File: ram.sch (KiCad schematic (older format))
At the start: 16 parts, among them U10 41256, U11 41256, U12 41256, U13 41256, U14 41256, U7 41256, U8 41256, U9 41256

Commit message: Routing in progress
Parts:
- removed C10, C11, C12, C13, C14, C8, C9: 100n, Capacitor_SMD:C_0805_2012Metric_Pad1.18x1.45mm_HandSolder, symbol Device:C
- removed U10, U11, U12, U13, U14, U7, U8, U9: 41256, Package_DIP:DIP-16_W7.62mm_Socket, symbol 41256:41256
- added U6: AS6C4008, Package_DIP:DIP-32_W15.24mm_Socket_LongPads, symbol AS6C4008:AS6C4008
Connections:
- net labels added: a0, a1, a10, a11, a12, a13, a14, a15, a16, a17, a18, a2, a3, a4, a5, a6, a7, a8, a9, a[0..18], ~SRAM_CE, ~sram_ce
- net labels removed: MultiplexedAddressBus, m0, m1, m2, m3, m4, m5, m6, m7, m8, m[0..8], ~CAS_64K, ~RAS
- wire segments 218 -> 40
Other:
- note removed: "WE NEED TO USE 41256 RAM CHIPS AS THEIR INTERNAL MATRIX IS\nORGANIZED IN 256 ROWS BY 1024 COLUMNS AND THUS ONLY NEED\nROWS A0-A7 FOR RAS-ONLY REFRESH (WHICH IS WHAT TED PRODUCES).\n\n44256 ARE GENERALLY ORGANIZED IN 512 ROWS AND WOULD NEED\nA MUCH MORE COMPLEX REFRESH LOGIC, IN ORDER TO REFRESH THE\nPAGES THAT ARE CURRENTLY NOT SELECTED."
- moved on the sheet: C7

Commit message: More routing
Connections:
- net d0: now also U6.15 (D2); no longer U6.13 (D0)
- net d2: now also U6.13 (D0); no longer U6.15 (D2)
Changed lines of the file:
@@
 d[0..7]
 Text Label 7340 4740 0    50   ~ 0
-d0
+d2
 Text Label 7340 4840 0    50   ~ 0
 d1
 Text Label 7340 4940 0    50   ~ 0
-d2
-Text Label 9730 4640 2    50   ~ 0
-d7
-Text Label 9730 4740 2    50   ~ 0
-d6
+d0
 Text Label 9730 4840 2    50   ~ 0
 d5
@@
 Wire Wire Line
 	9380 4540 9775 4540
+Text Label 9730 4040 2    50   ~ 0
+a6
+Text Label 9730 4240 2    50   ~ 0
+a4
 Wire Bus Line
 	7240 4640 7240 5670
@@
 Wire Bus Line
 	7240 2895 7240 4540
-Text Label 9730 4040 2    50   ~ 0
-a6
-Text Label 9730 4240 2    50   ~ 0
-a4
+Text Label 9730 4740 2    50   ~ 0
+d6
+Text Label 9730 4640 2    50   ~ 0
+d7
 $EndSCHEMATC

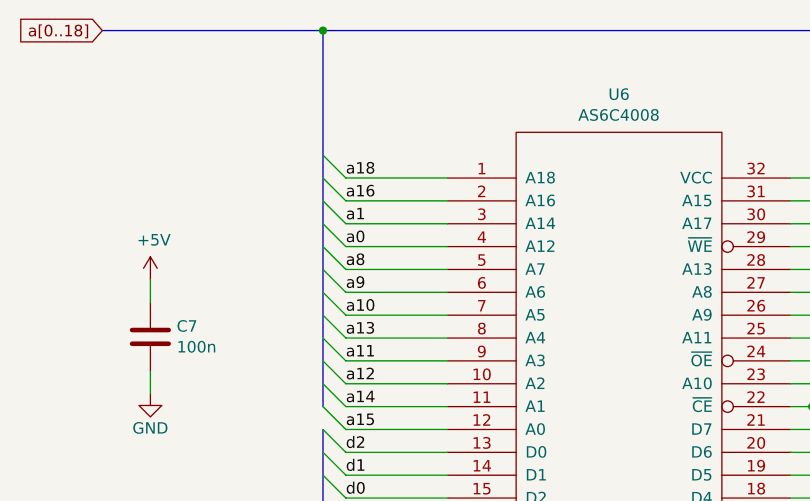
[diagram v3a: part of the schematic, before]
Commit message: Relabel all components
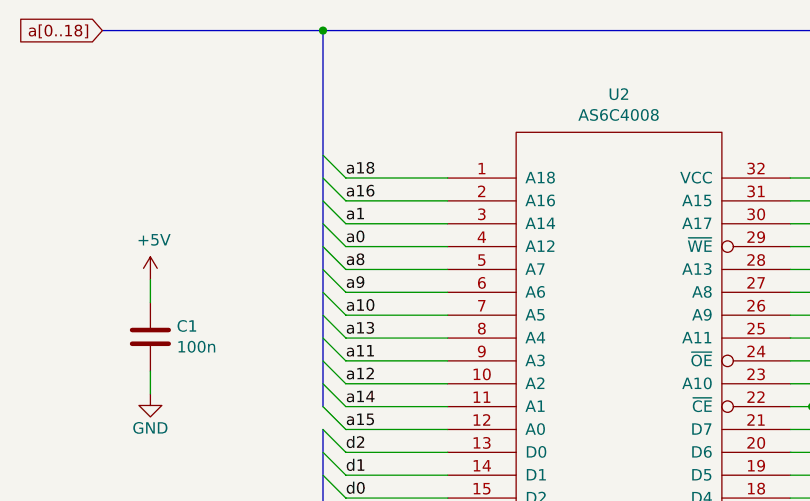
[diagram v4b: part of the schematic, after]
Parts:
- renumbered C7 to C1, U6 to U2
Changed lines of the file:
@@
 P 6485 4235
 AR Path="/63BD05FA" Ref="C?"  Part="1"
-AR Path="/62E48B71/63BD05FA" Ref="C7"  Part="1"
+AR Path="/62E48B71/63BD05FA" Ref="C1"  Part="1"
 AR Path="/63A22C28/63BD05FA" Ref="C?"  Part="1"
-F 0 "C7" H 6600 4281 50  0000 L CNN
+F 0 "C1" H 6600 4281 50  0000 L CNN
 F 1 "100n" H 6600 4190 50  0000 L CNN
 F 2 "Capacitor_SMD:C_0805_2012Metric_Pad1.18x1.45mm_HandSolder" H 6523 4085 50  0001 C CNN
@@
 P 6485 4485
 AR Path="/63BD0600" Ref="#PWR?"  Part="1"
-AR Path="/62E48B71/63BD0600" Ref="#PWR06"  Part="1"
+AR Path="/62E48B71/63BD0600" Ref="#PWR07"  Part="1"
 AR Path="/63A22C28/63BD0600" Ref="#PWR?"  Part="1"
-F 0 "#PWR06" H 6485 4235 50  0001 C CNN
+F 0 "#PWR07" H 6485 4235 50  0001 C CNN
 F 1 "GND" H 6485 4335 50  0000 C CNN
 F 2 "" H 6485 4485 50  0001 C CNN
@@
 P 6485 3985
 AR Path="/63BD0608" Ref="#PWR?"  Part="1"
-AR Path="/62E48B71/63BD0608" Ref="#PWR03"  Part="1"
+AR Path="/62E48B71/63BD0608" Ref="#PWR06"  Part="1"
 AR Path="/63A22C28/63BD0608" Ref="#PWR?"  Part="1"
-F 0 "#PWR03" H 6485 3835 50  0001 C CNN
+F 0 "#PWR06" H 6485 3835 50  0001 C CNN
 F 1 "+5V" H 6500 4158 50  0000 C CNN
 F 2 "" H 6485 3985 50  0001 C CNN
@@
 $EndComp
 $Comp
-L AS6C4008:AS6C4008 U6
+L AS6C4008:AS6C4008 U2
 U 1 1 63F5A21F
 P 8535 4290
-F 0 "U6" H 8535 5405 50  0000 C CNN
+F 0 "U2" H 8535 5405 50  0000 C CNN
 F 1 "AS6C4008" H 8535 5314 50  0000 C CNN
 F 2 "Package_DIP:DIP-32_W15.24mm_Socket_LongPads" H 8535 4290 50  0001 C CNN
@@
 P 7605 5385
 AR Path="/63FAC74C" Ref="#PWR?"  Part="1"
-AR Path="/62E48B71/63FAC74C" Ref="#PWR07"  Part="1"
+AR Path="/62E48B71/63FAC74C" Ref="#PWR08"  Part="1"
 AR Path="/63A22C28/63FAC74C" Ref="#PWR?"  Part="1"
-F 0 "#PWR07" H 7605 5135 50  0001 C CNN
+F 0 "#PWR08" H 7605 5135 50  0001 C CNN
 F 1 "GND" H 7605 5235 50  0000 C CNN
 F 2 "" H 7605 5385 50  0001 C CNN
@@
 P 9465 3195
 AR Path="/6400E4BF" Ref="#PWR?"  Part="1"
-AR Path="/62E48B71/6400E4BF" Ref="#PWR08"  Part="1"
+AR Path="/62E48B71/6400E4BF" Ref="#PWR09"  Part="1"
 AR Path="/63A22C28/6400E4BF" Ref="#PWR?"  Part="1"
-F 0 "#PWR08" H 9465 3045 50  0001 C CNN
+F 0 "#PWR09" H 9465 3045 50  0001 C CNN
 F 1 "+5V" H 9480 3368 50  0000 C CNN
 F 2 "" H 9465 3195 50  0001 C CNN

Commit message: More rerouting
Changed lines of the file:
@@
 Text GLabel 6275 2895 0    50   Input ~ 0
 a[0..18]
-Text Label 9730 4540 2    50   ~ 0
-~sram_ce
-Wire Wire Line
-	9285 4340 9380 4340
-Wire Wire Line
-	9380 4340 9380 4540
-Connection ~ 9380 4540
-Wire Wire Line
-	9380 4540 9285 4540
 Text GLabel 9955 4440 2    50   Input ~ 0
 ~SRAM_CE
@@
 Wire Wire Line
 	9775 4440 9955 4440
-Wire Wire Line
-	9380 4540 9775 4540
 Text Label 9730 4040 2    50   ~ 0
 a6
@@
 Text Label 9730 4640 2    50   ~ 0
 d7
+Wire Wire Line
+	9285 4540 9465 4540
+Wire Wire Line
+	9285 4340 9465 4340
+Wire Wire Line
+	9465 4340 9465 4540
 Wire Bus Line
 	7240 4640 7240 5670
@@
 Wire Bus Line
 	7240 2895 7240 4540
+Connection ~ 9465 4540
+Wire Wire Line
+	9465 4540 9775 4540
 $EndSCHEMATC

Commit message: Add part numbers
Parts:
- C1: LCSC (none) -> C49678
- U2: MouserPN (none) -> 913-AS6C4008-55PCN; Notes (none) -> -55PIN is also fine
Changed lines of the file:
@@
 F 2 "Capacitor_SMD:C_0805_2012Metric_Pad1.18x1.45mm_HandSolder" H 6523 4085 50  0001 C CNN
 F 3 "~" H 6485 4235 50  0001 C CNN
+F 4 "C49678" H 6485 4235 50  0001 C CNN "LCSC"
 	1    6485 4235
 	1    0    0    -1
@@
 F 2 "Package_DIP:DIP-32_W15.24mm_Socket_LongPads" H 8535 4290 50  0001 C CNN
 F 3 "DOCUMENTATION" H 8535 4290 50  0001 C CNN
+F 4 "913-AS6C4008-55PCN" H 8535 4290 50  0001 C CNN "MouserPN"
+F 5 "-55PIN is also fine" H 8535 4290 50  0001 C CNN "Notes"
 	1    8535 4290
 	1    0    0    -1
